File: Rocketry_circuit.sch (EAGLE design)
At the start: 6 parts

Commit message: Added wiring, still to figure out the RF-LORA-915-D data protocol
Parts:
- added ANT1, ANT2: ANTENNA, adafruit:ANTENNA
- added R1, R2: (no value), ngspice-simulation:R
- added U$6: RF-LORA-915-D, RF-LORA-915-D:RF-LORA-915-D
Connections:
- new net +3V3: BRKOUT1.VIN, R1.2, R2.2, U$2.VIN, U$3.3.3V, U$4.VCC, U$5.VCC, U$6.VCC
- new net +5V: U$1.VIN
- new net GND: BRKOUT1.GND, BRKOUT1.PS0, BRKOUT1.PS1, U$1.GND1, U$2.GND, U$2.SDO, U$3.GND, U$4.GND, U$5.GND, U$6.GND
- new net N$1: BRKOUT1.SCL, R2.1, U$1.19-A5/SCL0, U$2.SCK
- new net N$10: U$1.37-PWM
- new net N$2: BRKOUT1.SDA, R1.1, U$1.18-A4/SDA0, U$2.SDI
- new net N$3: ANT1.FEED, U$4.ANT
- new net N$4: U$1.0-RX1/CS1/CRX2, U$5.RX
- new net N$5: U$1.1-TX1/MISO1/CTX2, U$5.TX
- new net N$6: U$1.21-A7/RX5/BCLK1, U$3.X
- new net N$7: U$1.22-A8/CTX1, U$3.Y
- new net N$8: U$1.23-A9/CRX1/MCLK1, U$3.Z
- new net N$9: ANT2.FEED, U$6.ANT
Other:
- note added: "GROUND STATION"
- note added: "ONBOARD"
- note added: "SERVO"
- note added: "i2c address select LSB ->"

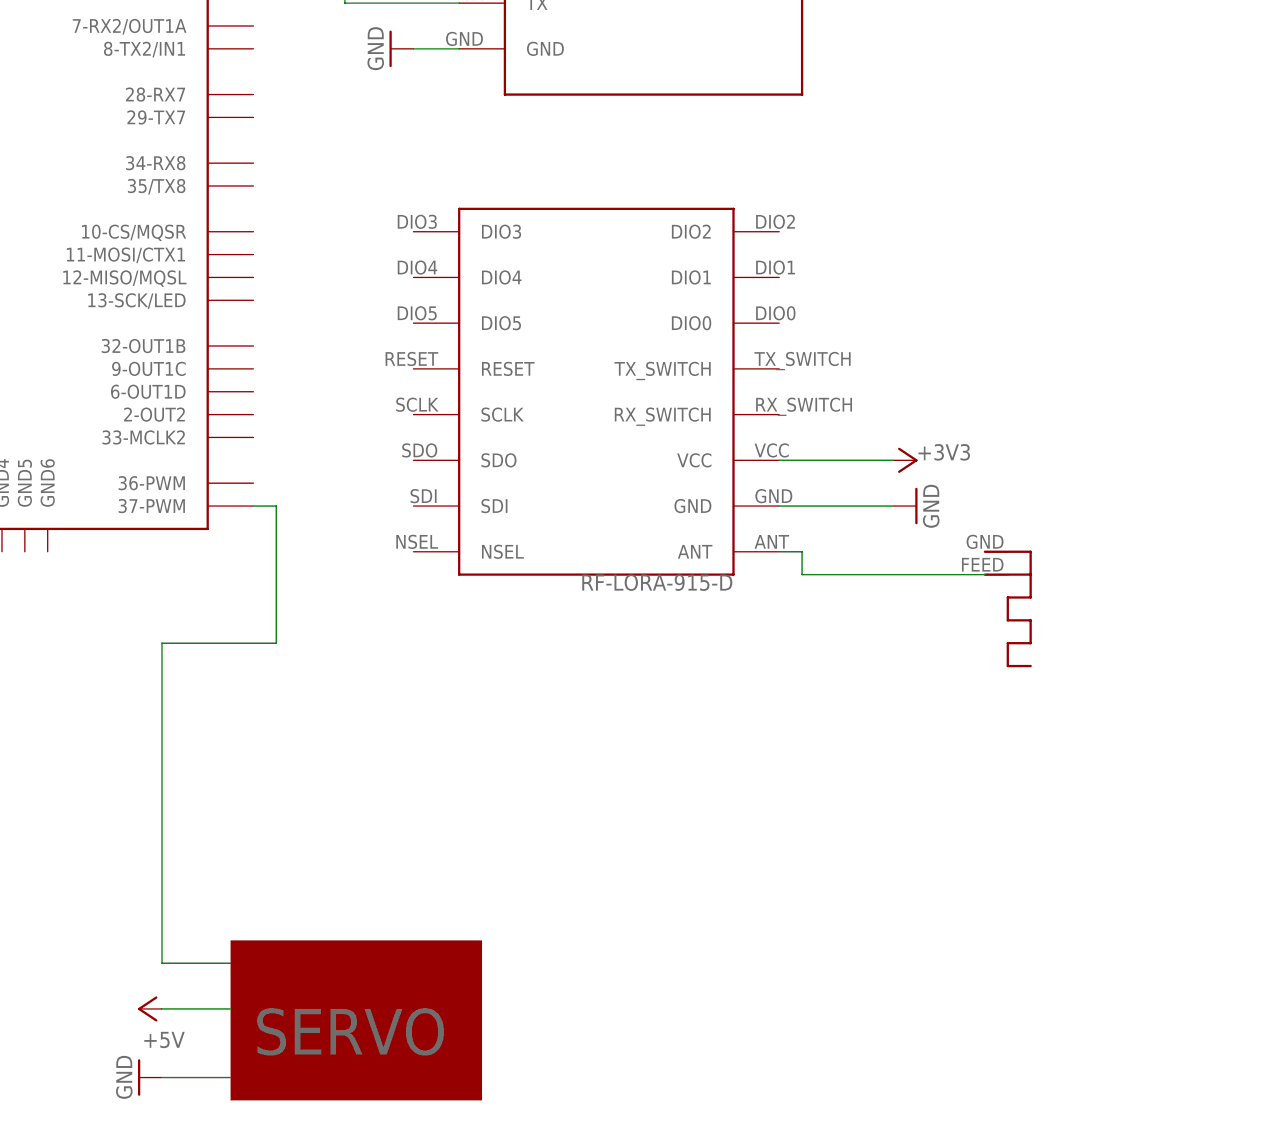
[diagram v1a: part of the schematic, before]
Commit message: Wired in the RF-LORA-915-D - Over SPI
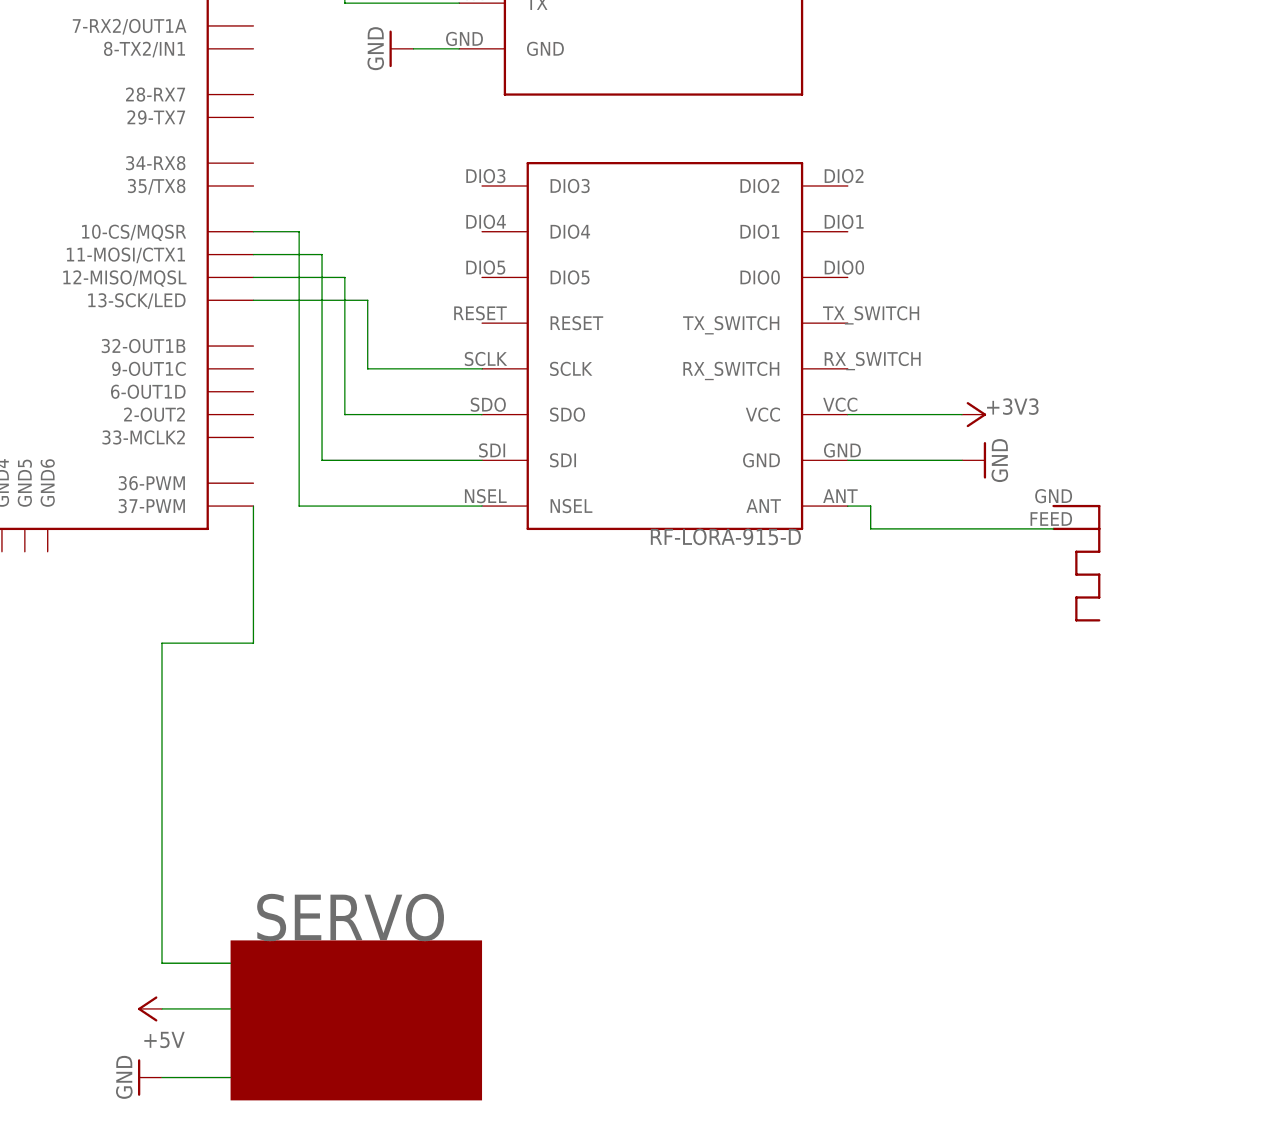
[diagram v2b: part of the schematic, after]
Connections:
- new net N$11: U$1.10-CS/MQSR, U$4.NSEL
- new net N$12: U$1.11-MOSI/CTX1, U$4.SDI
- new net N$13: U$1.12-MISO/MQSL, U$4.SDO
- new net N$14: U$1.13-SCK/LED, U$4.SCLK
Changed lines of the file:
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@@
 <text x="335.28" y="223.52" size="6.4516" layer="103">GROUND STATION</text>
 <rectangle x1="88.9" y1="12.7" x2="116.84" y2="30.48" layer="94"/>
-<text x="91.44" y="17.78" size="5.08" layer="95">SERVO</text>
+<text x="91.44" y="30.48" size="5.08" layer="95">SERVO</text>
 </plain>
 <instances>
@@
 <instance part="U$2" gate="G$1" x="-58.42" y="104.14" smashed="yes" rot="R180"/>
 <instance part="U$3" gate="G$1" x="-66.04" y="63.5" smashed="yes" rot="R180"/>
-<instance part="U$4" gate="G$1" x="129.54" y="91.44" smashed="yes" rot="R180"/>
+<instance part="U$4" gate="G$1" x="137.16" y="96.52" smashed="yes" rot="R180"/>
 <instance part="U$5" gate="G$1" x="129.54" y="137.16" smashed="yes"/>
 <instance part="+3V1" gate="G$1" x="-22.86" y="187.96" smashed="yes">
@@
 <attribute name="VALUE" x="-38.1" y="93.98" size="1.778" layer="96"/>
 </instance>
-<instance part="GND6" gate="1" x="165.1" y="78.74" smashed="yes" rot="R90">
-<attribute name="VALUE" x="167.64" y="76.2" size="1.778" layer="96" rot="R90"/>
-</instance>
-<instance part="+3V4" gate="G$1" x="165.1" y="83.82" smashed="yes" rot="R270">
-<attribute name="VALUE" x="165.1" y="83.82" size="1.778" layer="96"/>
-</instance>
-<instance part="ANT1" gate="G$1" x="172.72" y="71.12" smashed="yes" rot="MR90"/>
+<instance part="GND6" gate="1" x="172.72" y="83.82" smashed="yes" rot="R90">
+<attribute name="VALUE" x="175.26" y="81.28" size="1.778" layer="96" rot="R90"/>
+</instance>
+<instance part="+3V4" gate="G$1" x="172.72" y="88.9" smashed="yes" rot="R270">
+<attribute name="VALUE" x="172.72" y="88.9" size="1.778" layer="96"/>
+</instance>
+<instance part="ANT1" gate="G$1" x="180.34" y="76.2" smashed="yes" rot="MR90"/>
 <instance part="GND7" gate="1" x="106.68" y="129.54" smashed="yes" rot="R270">
 <attribute name="VALUE" x="104.14" y="132.08" size="1.778" layer="96" rot="R270"/>
@@
 <pinref part="+3V4" gate="G$1" pin="+3V3"/>
 <pinref part="U$4" gate="G$1" pin="VCC"/>
-<wire x1="162.56" y1="83.82" x2="149.86" y2="83.82" width="0.254" layer="91"/>
+<wire x1="170.18" y1="88.9" x2="157.48" y2="88.9" width="0.254" layer="91"/>
 </segment>
 <segment>
@@
 <pinref part="GND6" gate="1" pin="GND"/>
 <pinref part="U$4" gate="G$1" pin="GND"/>
-<wire x1="162.56" y1="78.74" x2="149.86" y2="78.74" width="0.254" layer="91"/>
+<wire x1="170.18" y1="83.82" x2="157.48" y2="83.82" width="0.254" layer="91"/>
 </segment>
 <segment>
@@
 <segment>
 <pinref part="ANT1" gate="G$1" pin="FEED"/>
-<wire x1="172.72" y1="71.12" x2="152.4" y2="71.12" width="0.254" layer="91"/>
-<wire x1="152.4" y1="71.12" x2="152.4" y2="73.66" width="0.254" layer="91"/>
+<wire x1="180.34" y1="76.2" x2="160.02" y2="76.2" width="0.254" layer="91"/>
+<wire x1="160.02" y1="76.2" x2="160.02" y2="78.74" width="0.254" layer="91"/>
 <pinref part="U$4" gate="G$1" pin="ANT"/>
-<wire x1="152.4" y1="73.66" x2="149.86" y2="73.66" width="0.254" layer="91"/>
+<wire x1="160.02" y1="78.74" x2="157.48" y2="78.74" width="0.254" layer="91"/>
 </segment>
 </net>
@@
 <wire x1="88.9" y1="27.94" x2="81.28" y2="27.94" width="0.254" layer="91"/>
 <wire x1="81.28" y1="27.94" x2="81.28" y2="63.5" width="0.254" layer="91"/>
-<wire x1="81.28" y1="63.5" x2="93.98" y2="63.5" width="0.254" layer="91"/>
+<wire x1="81.28" y1="63.5" x2="91.44" y2="63.5" width="0.254" layer="91"/>
 <pinref part="U$1" gate="G$1" pin="37-PWM"/>
-<wire x1="93.98" y1="63.5" x2="93.98" y2="78.74" width="0.254" layer="91"/>
-<wire x1="93.98" y1="78.74" x2="91.44" y2="78.74" width="0.254" layer="91"/>
-</segment>
-</net>
+<wire x1="91.44" y1="63.5" x2="91.44" y2="78.74" width="0.254" layer="91"/>
+</segment>
+</net>
+<net name="N$11" class="0">
+<segment>
+<pinref part="U$4" gate="G$1" pin="NSEL"/>
+<wire x1="116.84" y1="78.74" x2="96.52" y2="78.74" width="0.1524" layer="91"/>
+<wire x1="96.52" y1="78.74" x2="96.52" y2="109.22" width="0.1524" layer="91"/>
+<pinref part="U$1" gate="G$1" pin="10-CS/MQSR"/>
+<wire x1="96.52" y1="109.22" x2="91.44" y2="109.22" width="0.1524" layer="91"/>
+</segment>
+</net>
+<net name="N$12" class="0">
+<segment>
+<pinref part="U$4" gate="G$1" pin="SDI"/>
+<wire x1="116.84" y1="83.82" x2="99.06" y2="83.82" width="0.1524" layer="91"/>
+<wire x1="99.06" y1="83.82" x2="99.06" y2="106.68" width="0.1524" layer="91"/>
+<pinref part="U$1" gate="G$1" pin="11-MOSI/CTX1"/>
+<wire x1="99.06" y1="106.68" x2="91.44" y2="106.68" width="0.1524" layer="91"/>
+</segment>
+</net>
+<net name="N$13" class="0">
+<segment>
+<pinref part="U$4" gate="G$1" pin="SDO"/>
+<wire x1="116.84" y1="88.9" x2="101.6" y2="88.9" width="0.1524" layer="91"/>
+<wire x1="101.6" y1="88.9" x2="101.6" y2="104.14" width="0.1524" layer="91"/>
+<pinref part="U$1" gate="G$1" pin="12-MISO/MQSL"/>
+<wire x1="101.6" y1="104.14" x2="91.44" y2="104.14" width="0.1524" layer="91"/>
+</segment>
+</net>
+<net name="N$14" class="0">
+<segment>
+<pinref part="U$1" gate="G$1" pin="13-SCK/LED"/>
+<wire x1="91.44" y1="101.6" x2="104.14" y2="101.6" width="0.1524" layer="91"/>
+<pinref part="U$4" gate="G$1" pin="SCLK"/>
+<wire x1="104.14" y1="101.6" x2="104.14" y2="93.98" width="0.1524" layer="91"/>
+<wire x1="104.14" y1="93.98" x2="116.84" y2="93.98" width="0.1524" layer="91"/>
+</segment>
+</net>

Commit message: Replaced NEO6M with NEO-M9N and wired it up.
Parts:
- added ANT3: ANTENNA, adafruit:ANTENNA
- added U$7: TEENSY40, teensy:TEENSY40
- R1, R2: value (none) -> 2.2k
- U$5: value NEO6M -> NEO-M9N; device NEO6M:NEO6M -> NEOM9N:NEO-M9N
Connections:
- removed net N$4 (its old number): U$1.0-RX1/CS1/CRX2, U$5.RX
- removed net N$5 (its old number): U$1.1-TX1/MISO1/CTX2, U$5.TX
- new net N$15: ANT3.FEED, U$5.ANT
- new net N$16: U$6.NSEL, U$7.10-CS
- new net N$17: U$6.SDO, U$7.12-MISO/MQSL
- new net N$18: U$6.SDI, U$7.11-MOSI/CTX1
- new net N$19: U$6.SCLK, U$7.13-SCK/CRX1/LED
- new net N$7: U$1.24-A10/TX6/SCL2, U$5.SCL
- new net N$8: U$1.25-A11/RX6/SDA2, U$5.SDA
- net +3V3: now also U$5.3.3V; no longer U$5.VCC
- net +5V: now also U$7.VUSB
- net GND: now also ANT1.GND, ANT2.GND, ANT3.GND, U$5.GND2, U$7.GND1; no longer U$5.GND
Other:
- note added: "Any microcontroller , e.g. arduino nano"
- note added: "Inbuilt 2.2k pull up resistors"

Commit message: Updated library files (accuracy) and added 3D models. .brd file added
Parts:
- removed ANT1, ANT2, ANT3: ANTENNA, adafruit:ANTENNA
- removed R2: 2.2k, ngspice-simulation:R
- removed U$4, U$6: RF-LORA-915-D, RF-LORA-915-D:RF-LORA-915-D
- removed U$5: NEO-M9N, NEOM9N:NEO-M9N
- removed U$7: TEENSY40, teensy:TEENSY40
- added R3: 2.2k, adafruit:R-US_0207/5V
- added SG1: EFBAA40D101, buzzer:EFBAA40D101
- R1: device ngspice-simulation:R -> adafruit:R-US_0207/5V
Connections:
- removed net N$1: BRKOUT1.SCL, R2.1, U$1.19-A5/SCL0, U$2.SCK
- removed net N$10: U$1.37-PWM
- removed net N$11: U$1.10-CS/MQSR, U$4.NSEL
- removed net N$12: U$1.11-MOSI/CTX1, U$4.SDI
- removed net N$13: U$1.12-MISO/MQSL, U$4.SDO
- removed net N$14: U$1.13-SCK/LED, U$4.SCLK
- removed net N$15: ANT3.FEED, U$5.ANT
- removed net N$16: U$6.NSEL, U$7.10-CS
- removed net N$17: U$6.SDO, U$7.12-MISO/MQSL
- removed net N$18: U$6.SDI, U$7.11-MOSI/CTX1
- removed net N$19: U$6.SCLK, U$7.13-SCK/CRX1/LED
- removed net N$2: BRKOUT1.SDA, R1.1, U$1.18-A4/SDA0, U$2.SDI
- removed net N$4: U$1.21-A7/RX5/BCLK1, U$3.X
- removed net N$6: U$1.23-A9/CRX1/MCLK1, U$3.Z
- removed net N$7: U$1.24-A10/TX6/SCL2, U$5.SCL
- removed net N$8: U$1.25-A11/RX6/SDA2, U$5.SDA
- removed net N$9: ANT2.FEED, U$6.ANT
- net +3V3: now also R3.2; no longer R2.2, U$2.VIN, U$3.3.3V, U$4.VCC, U$5.3.3V, U$6.VCC
- net +5V: no longer U$7.VUSB
- net GND: no longer ANT1.GND, ANT2.GND, ANT3.GND, U$2.GND, U$2.SDO, U$3.GND, U$4.GND, U$5.GND2, U$6.GND, U$7.GND1
- net N$3: now also BRKOUT1.SDA, R1.1, U$1.26-A12/MOSI1; no longer ANT1.FEED, U$4.ANT
- net N$5: now also BRKOUT1.SCL, R3.1, U$1.25-A11/RX6/SDA2; no longer U$1.22-A8/CTX1, U$3.Y
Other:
- note removed: "Any microcontroller , e.g. arduino nano"
- note removed: "GROUND STATION"
- note removed: "Inbuilt 2.2k pull up resistors"
- note removed: "SERVO"
